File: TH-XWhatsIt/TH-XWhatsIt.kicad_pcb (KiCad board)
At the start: 2 copper layers, 178 x 115.5 mm, 48 parts, among them J1 COLUMNS, J10 DISPLAYWRITER PLUGBOARD CONNE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, J11 DISPLAYWRITER PLUGBOARD ROWS, J12 EXPANSION HEADER, J13 Conn_01x02, J2 ROWS, J3 MODEL F PLUGBOARD COLUMNS, J4 MODEL F PLUGBOARD CONNECTOR, J5 MODEL F PLUGBOARD ROWS, J6 BEAMSPRING PLUGBOARD COLUMNS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

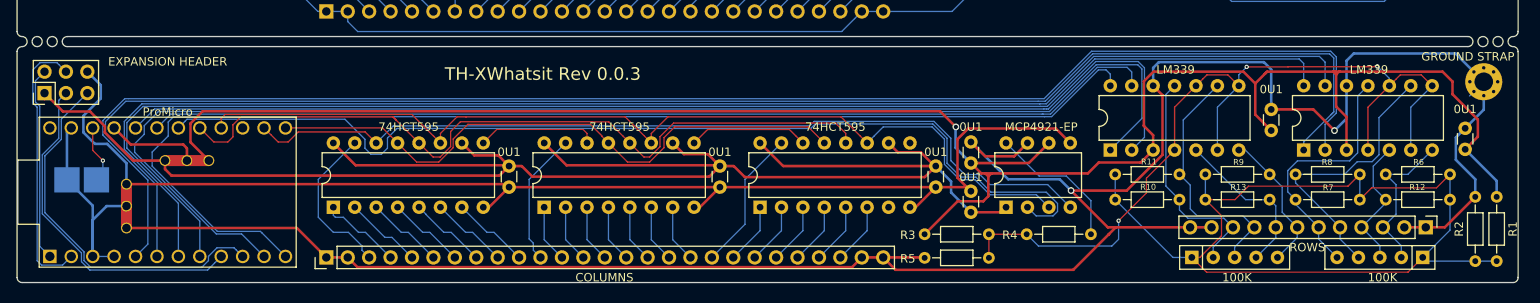
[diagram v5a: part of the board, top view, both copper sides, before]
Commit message: repositioned chips and resistors to make space for beamspring connector
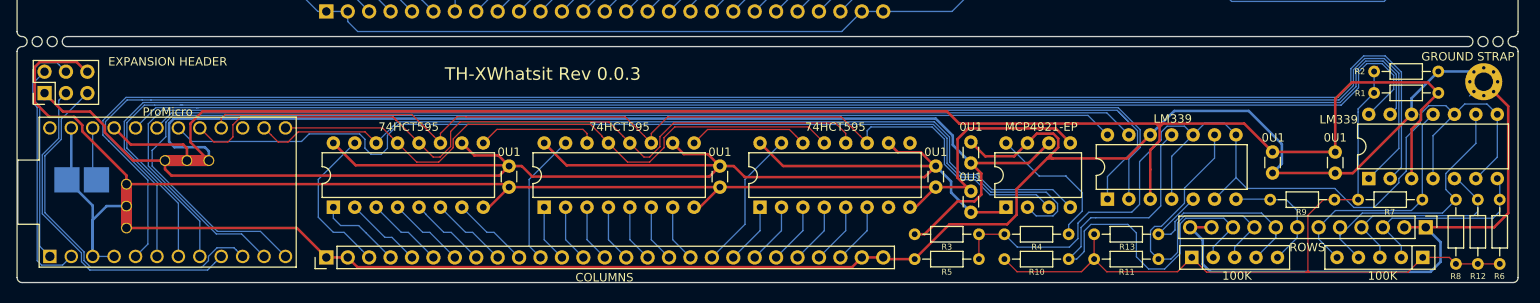
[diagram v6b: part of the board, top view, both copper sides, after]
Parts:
- moved R2 25.5 mm to (214.5, 123.8), turned to 0 degrees
- moved C9 16.3 mm to (209.9, 135.9), turned to 90 degrees
- moved R9 15.6 mm to (209.8, 139.0), turned to 180 degrees
- moved R8 15.6 mm to (224.2, 146.6), turned to 90 degrees
- moved R10 14.9 mm to (170.7, 146.1)
- moved R1 14.1 mm to (222.1, 126.3), turned to 180 degrees
- moved R13 13.8 mm to (181.3, 143.1)
- moved R6 12.1 mm to (229.4, 146.6), turned to 90 degrees
- moved R11 10.4 mm to (181.3, 146.1)
- moved U1 8.43 mm to (213.9, 136.5)
- moved R12 8.30 mm to (226.8, 146.6), turned to 90 degrees
- moved C10 7.54 mm to (202.5, 135.8), turned to 90 degrees
- moved U6 5.83 mm to (182.9, 138.9)
- moved R4 2.64 mm to (170.7, 143.1)
- moved R5 1.19 mm to (160.0, 146.1)
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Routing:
- net +5VA: track 231.0 -> 316.6 mm, vias 1 -> 0
- net SENSE8: track 27.6 -> 59.8 mm
- net SETPOINT: track 100.7 -> 123.1 mm, vias 3 -> 0
- net ROW3: track 165.0 -> 180.4 mm
- net BIAS: track 111.0 -> 96.5 mm
- net ROW4: track 167.4 -> 179.3 mm
- net ROW2: track 180.5 -> 191.2 mm
- net ROW1: track 180.5 -> 190.9 mm
- net SENSE6: track 30.0 -> 39.4 mm
- net GNDD: track 199.0 -> 208.3 mm
- net SENSE7: track 19.5 -> 28.2 mm
- net SENSE2: track 16.2 -> 24.3 mm
- net GND: track 35.8 -> 29.0 mm
- net SENSE1: track 18.6 -> 23.1 mm
- net ROW5: track 156.8 -> 153.3 mm
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
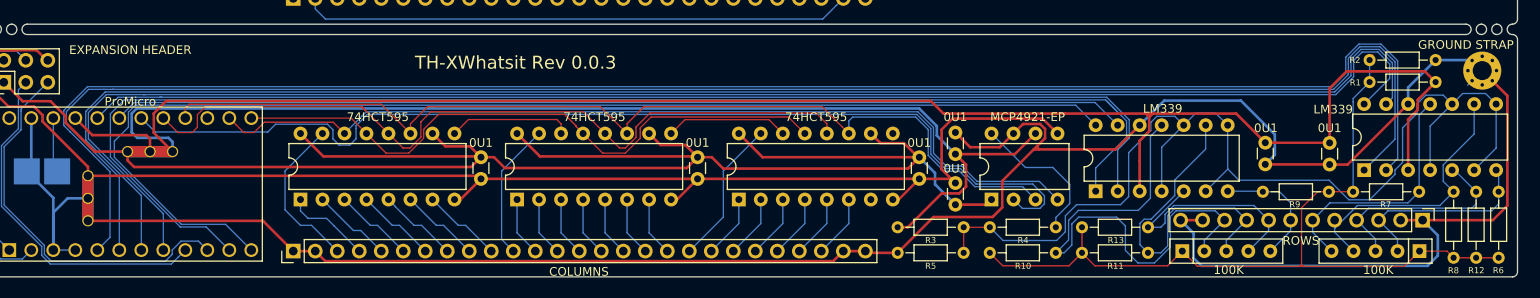
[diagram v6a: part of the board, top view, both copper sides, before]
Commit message: I'm just after realizing that this PCB was using the style where the component values are on silkscreen but not the RefDes. Making my changes match this style.
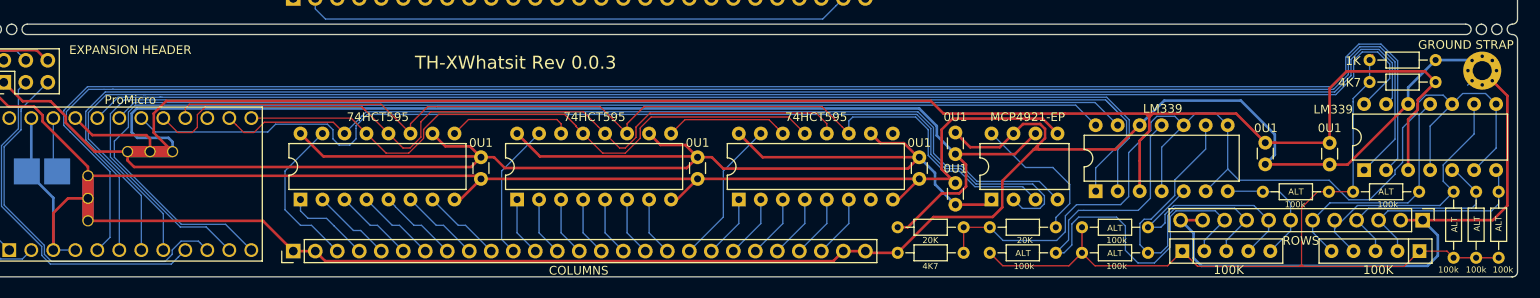
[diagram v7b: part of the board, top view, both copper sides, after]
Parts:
- R10, R11, R12, R13, R6, R7, R8, R9: value NM -> 100k
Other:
- board text added: "ALT"

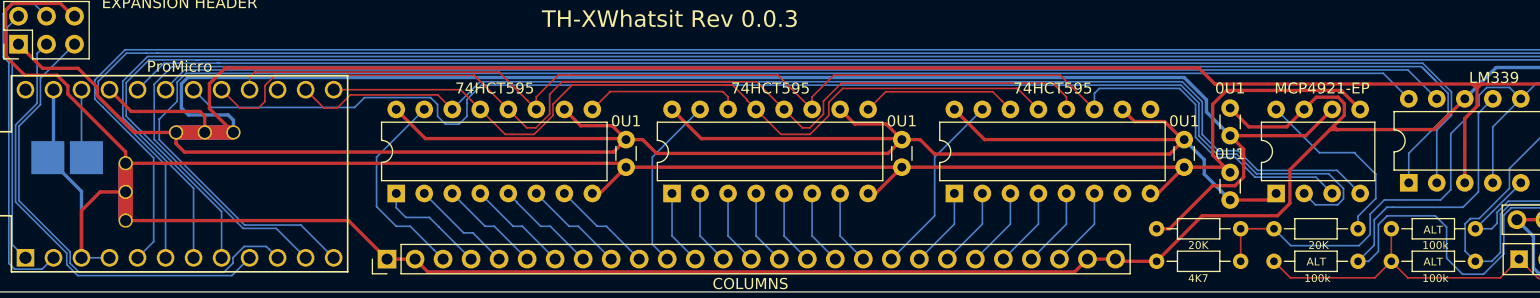
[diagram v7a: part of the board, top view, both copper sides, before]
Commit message: Made net ties thicker
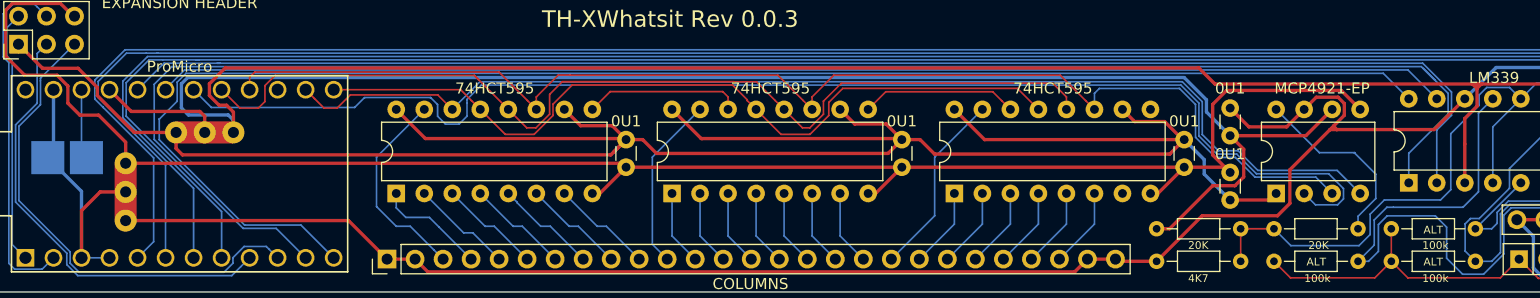
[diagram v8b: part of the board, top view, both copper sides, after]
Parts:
- NT1, NT2: footprint NetTie:NetTie-3_THT_Pad1.0mm -> TH-XWhatsIt:NetTie-3_THT_Pad1.0mm_mod_thicker
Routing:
- net +5VD: track 218.7 -> 220.7 mm
- net GNDD: track 208.3 -> 209.3 mm
